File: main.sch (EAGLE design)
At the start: 87 parts, among them Q1 5.8A/30V/35mΩ, Q2 5.8A/30V/35mΩ, Q3 2.5A/30V/105mΩ, U1 BQ24133_RGY_24, U2 SN65HVD32_D_8

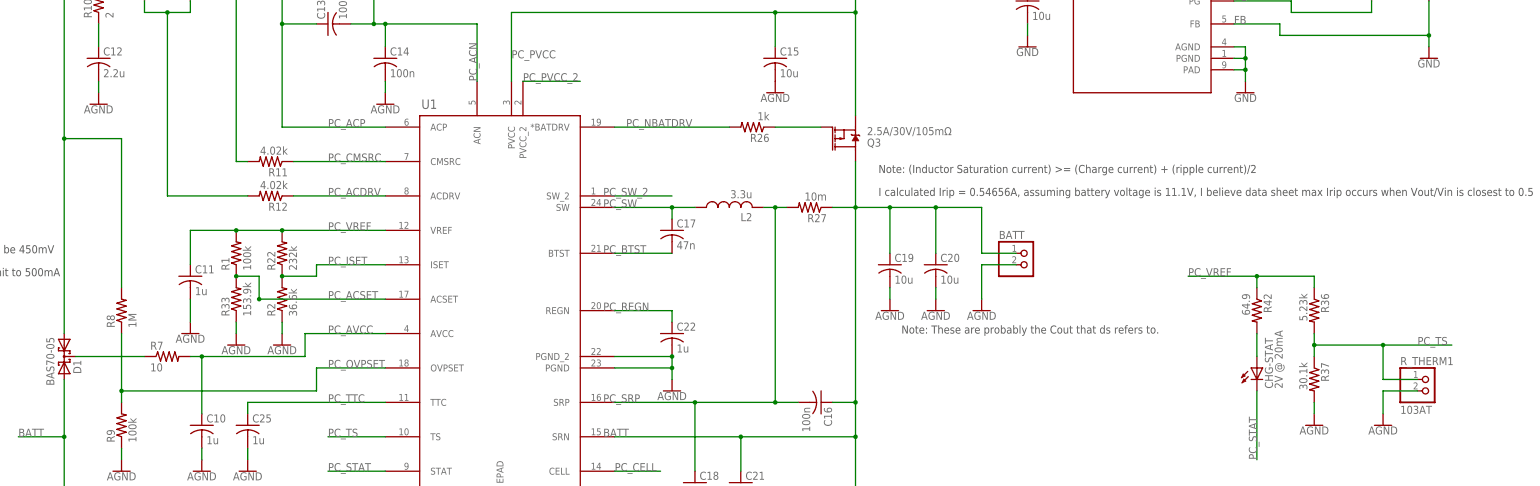
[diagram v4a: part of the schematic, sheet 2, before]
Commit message: Seperated grounds, added pullup to cell pin
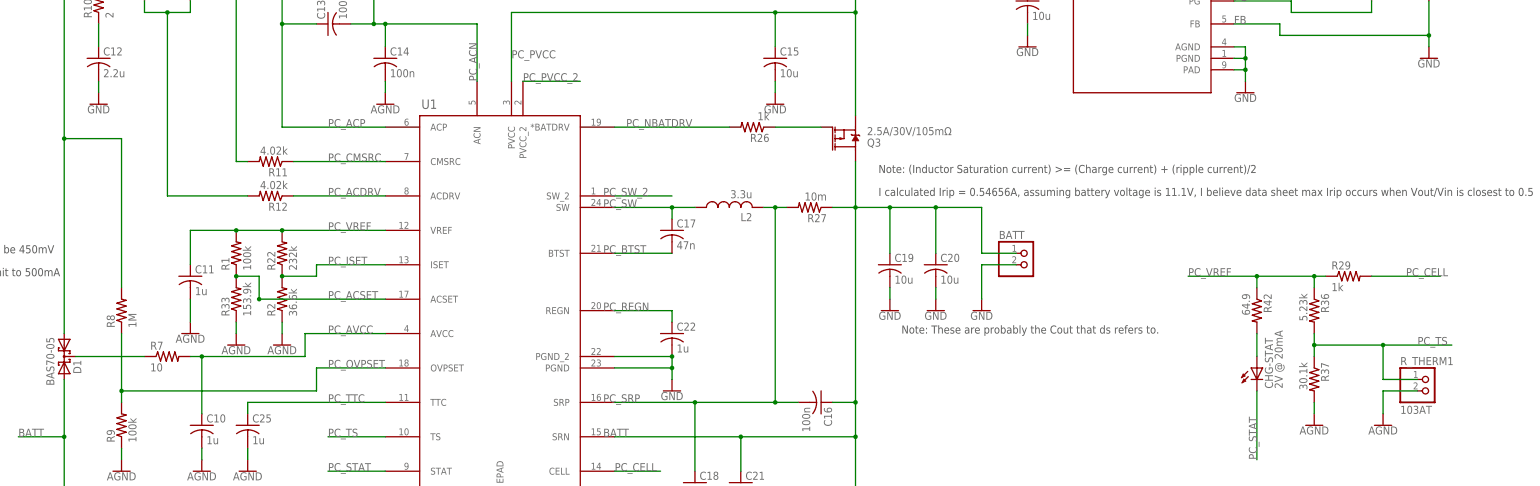
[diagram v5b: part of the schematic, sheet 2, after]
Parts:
- added R29: 1k, resistor:R-US_R0603
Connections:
- net AGND: no longer BATT.2, C12.2, C15.2, C19.2, C20.2, C22.2, U1.PGND, U1.PGND_2
- net GND: now also BATT.2, C12.2, C15.2, C19.2, C20.2, C22.2, U1.PGND, U1.PGND_2
- net PC_CELL: now also R29.2
- net PC_VREF: now also R29.1
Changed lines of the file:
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@@
 <part name="R31" library="resistor" library_urn="urn:adsk.eagle:library:348" deviceset="R-US_" device="R0603" package3d_urn="urn:adsk.eagle:package:26057/1" value="10k"/>
 <part name="SUPPLY6" library="SparkFun-PowerSymbols" deviceset="3.3V" device=""/>
-<part name="U$18" library="SparkFun-PowerSymbols" deviceset="AGND" device=""/>
-<part name="U$19" library="SparkFun-PowerSymbols" deviceset="AGND" device=""/>
-<part name="U$20" library="SparkFun-PowerSymbols" deviceset="AGND" device=""/>
-<part name="U$22" library="SparkFun-PowerSymbols" deviceset="AGND" device=""/>
-<part name="U$23" library="SparkFun-PowerSymbols" deviceset="AGND" device=""/>
-<part name="U$24" library="SparkFun-PowerSymbols" deviceset="AGND" device=""/>
 <part name="SUPPLY9" library="SparkFun-PowerSymbols" deviceset="3.3V" device=""/>
 <part name="GPIO" library="pinhead" library_urn="urn:adsk.eagle:library:325" deviceset="PINHD-1X10" device="" package3d_urn="urn:adsk.eagle:package:22406/2"/>
@@
 <part name="LED1" library="adafruit" deviceset="LED" device="CHIPLED_0603" value="2V @ 20mA"/>
 <part name="SUPPLY11" library="SparkFun-PowerSymbols" deviceset="3.3V" device=""/>
+<part name="GND20" library="SparkFun-PowerSymbols" deviceset="GND" device=""/>
+<part name="GND21" library="SparkFun-PowerSymbols" deviceset="GND" device=""/>
+<part name="GND22" library="SparkFun-PowerSymbols" deviceset="GND" device=""/>
+<part name="GND23" library="SparkFun-PowerSymbols" deviceset="GND" device=""/>
+<part name="GND25" library="SparkFun-PowerSymbols" deviceset="GND" device=""/>
+<part name="GND26" library="SparkFun-PowerSymbols" deviceset="GND" device=""/>
+<part name="R29" library="resistor" library_urn="urn:adsk.eagle:library:348" deviceset="R-US_" device="R0603" package3d_urn="urn:adsk.eagle:package:26057/1" value="1k"/>
 </parts>
 <sheets>
@@
 <instance part="U$15" gate="G$1" x="472.44" y="22.86"/>
 <instance part="U$17" gate="G$1" x="482.6" y="22.86"/>
-<instance part="U$18" gate="G$1" x="467.36" y="53.34"/>
-<instance part="U$19" gate="G$1" x="340.36" y="116.84"/>
-<instance part="U$20" gate="G$1" x="490.22" y="119.38"/>
-<instance part="U$22" gate="G$1" x="535.94" y="71.12"/>
-<instance part="U$23" gate="G$1" x="525.78" y="71.12"/>
-<instance part="U$24" gate="G$1" x="515.62" y="71.12"/>
+<instance part="GND20" gate="1" x="490.22" y="116.84"/>
+<instance part="GND21" gate="1" x="340.36" y="116.84"/>
+<instance part="GND22" gate="1" x="467.36" y="53.34"/>
+<instance part="GND23" gate="1" x="515.62" y="71.12"/>
+<instance part="GND25" gate="1" x="525.78" y="71.12"/>
+<instance part="GND26" gate="1" x="535.94" y="71.12"/>
+<instance part="R29" gate="G$1" x="617.22" y="78.74"/>
 </instances>
 <busses>
@@
 <wire x1="454.66" y1="12.7" x2="454.66" y2="15.24" width="0.1524" layer="91"/>
 <wire x1="454.66" y1="15.24" x2="447.04" y2="15.24" width="0.1524" layer="91"/>
+</segment>
+<segment>
+<pinref part="C15" gate="G$1" pin="2"/>
+<pinref part="GND20" gate="1" pin="GND"/>
+<wire x1="490.22" y1="119.38" x2="490.22" y2="121.92" width="0.1524" layer="91"/>
+</segment>
+<segment>
+<pinref part="C12" gate="G$1" pin="2"/>
+<wire x1="340.36" y1="119.38" x2="340.36" y2="121.92" width="0.1524" layer="91"/>
+<pinref part="GND21" gate="1" pin="GND"/>
+</segment>
+<segment>
+<pinref part="U1" gate="A" pin="PGND"/>
+<pinref part="U1" gate="A" pin="PGND_2"/>
+<wire x1="454.66" y1="60.96" x2="467.36" y2="60.96" width="0.1524" layer="91"/>
+<wire x1="467.36" y1="60.96" x2="467.36" y2="58.42" width="0.1524" layer="91"/>
+<pinref part="C22" gate="G$1" pin="2"/>
+<junction x="467.36" y="60.96"/>
+<wire x1="467.36" y1="58.42" x2="467.36" y2="55.88" width="0.1524" layer="91"/>
+<wire x1="454.66" y1="58.42" x2="467.36" y2="58.42" width="0.1524" layer="91"/>
+<junction x="467.36" y="58.42"/>
+<pinref part="GND22" gate="1" pin="GND"/>
+</segment>
+<segment>
+<pinref part="C19" gate="G$1" pin="2"/>
+<wire x1="515.62" y1="73.66" x2="515.62" y2="76.2" width="0.1524" layer="91"/>
+<pinref part="GND23" gate="1" pin="GND"/>
+</segment>
+<segment>
+<pinref part="C20" gate="G$1" pin="2"/>
+<wire x1="525.78" y1="76.2" x2="525.78" y2="73.66" width="0.1524" layer="91"/>
+<pinref part="GND25" gate="1" pin="GND"/>
+</segment>
+<segment>
+<pinref part="BATT" gate="G$1" pin="2"/>
+<wire x1="543.56" y1="81.28" x2="535.94" y2="81.28" width="0.1524" layer="91"/>
+<wire x1="535.94" y1="81.28" x2="535.94" y2="73.66" width="0.1524" layer="91"/>
+<pinref part="GND26" gate="1" pin="GND"/>
 </segment>
 </net>
@@
 <junction x="596.9" y="78.74"/>
 <label x="581.66" y="78.74" size="1.778" layer="95"/>
+<pinref part="R29" gate="G$1" pin="1"/>
+<wire x1="609.6" y1="78.74" x2="612.14" y2="78.74" width="0.1524" layer="91"/>
+<junction x="609.6" y="78.74"/>
 </segment>
 </net>
@@
 <label x="454.66" y="35.56" size="1.778" layer="95"/>
 </segment>
+<segment>
+<pinref part="R29" gate="G$1" pin="2"/>
+<wire x1="622.3" y1="78.74" x2="637.54" y2="78.74" width="0.1524" layer="91"/>
+<label x="629.92" y="78.74" size="1.778" layer="95"/>
+</segment>
 </net>
 <net name="PC_PVCC_2" class="0">
@@
 <pinref part="U$17" gate="G$1" pin="AGND"/>
 </segment>
-<segment>
-<pinref part="U1" gate="A" pin="PGND"/>
-<pinref part="U1" gate="A" pin="PGND_2"/>
-<wire x1="454.66" y1="60.96" x2="467.36" y2="60.96" width="0.1524" layer="91"/>
-<wire x1="467.36" y1="60.96" x2="467.36" y2="58.42" width="0.1524" layer="91"/>
-<pinref part="C22" gate="G$1" pin="2"/>
-<junction x="467.36" y="60.96"/>
-<wire x1="467.36" y1="58.42" x2="467.36" y2="55.88" width="0.1524" layer="91"/>
-<wire x1="454.66" y1="58.42" x2="467.36" y2="58.42" width="0.1524" layer="91"/>
-<junction x="467.36" y="58.42"/>
-<pinref part="U$18" gate="G$1" pin="AGND"/>
-</segment>
-<segment>
-<pinref part="C12" gate="G$1" pin="2"/>
-<wire x1="340.36" y1="119.38" x2="340.36" y2="121.92" width="0.1524" layer="91"/>
-<pinref part="U$19" gate="G$1" pin="AGND"/>
-</segment>
-<segment>
-<pinref part="C15" gate="G$1" pin="2"/>
-<pinref part="U$20" gate="G$1" pin="AGND"/>
-</segment>
-<segment>
-<pinref part="BATT" gate="G$1" pin="2"/>
-<wire x1="543.56" y1="81.28" x2="535.94" y2="81.28" width="0.1524" layer="91"/>
-<wire x1="535.94" y1="81.28" x2="535.94" y2="73.66" width="0.1524" layer="91"/>
-<pinref part="U$22" gate="G$1" pin="AGND"/>
-</segment>
-<segment>
-<pinref part="C20" gate="G$1" pin="2"/>
-<wire x1="525.78" y1="76.2" x2="525.78" y2="73.66" width="0.1524" layer="91"/>
-<pinref part="U$23" gate="G$1" pin="AGND"/>
-</segment>
-<segment>
-<pinref part="C19" gate="G$1" pin="2"/>
-<wire x1="515.62" y1="73.66" x2="515.62" y2="76.2" width="0.1524" layer="91"/>
-<pinref part="U$24" gate="G$1" pin="AGND"/>
-</segment>
-</net>
+</net>

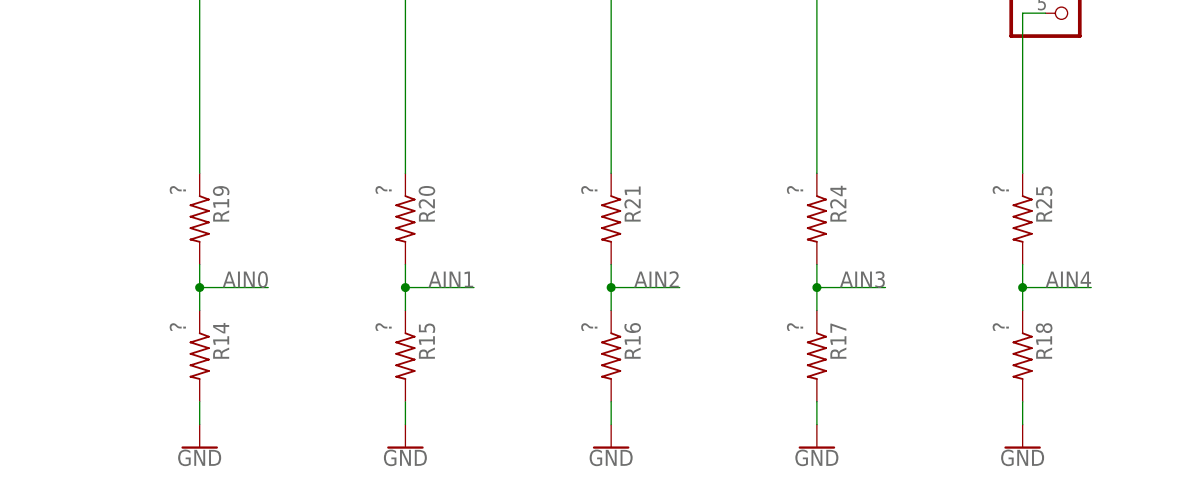
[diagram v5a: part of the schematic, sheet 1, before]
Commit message: Set adc voltage divider values
Used 100ohm output impedance of ducers and 3.5kohm limit in samd21 datasheet to arrive at the vdiv resistor values.
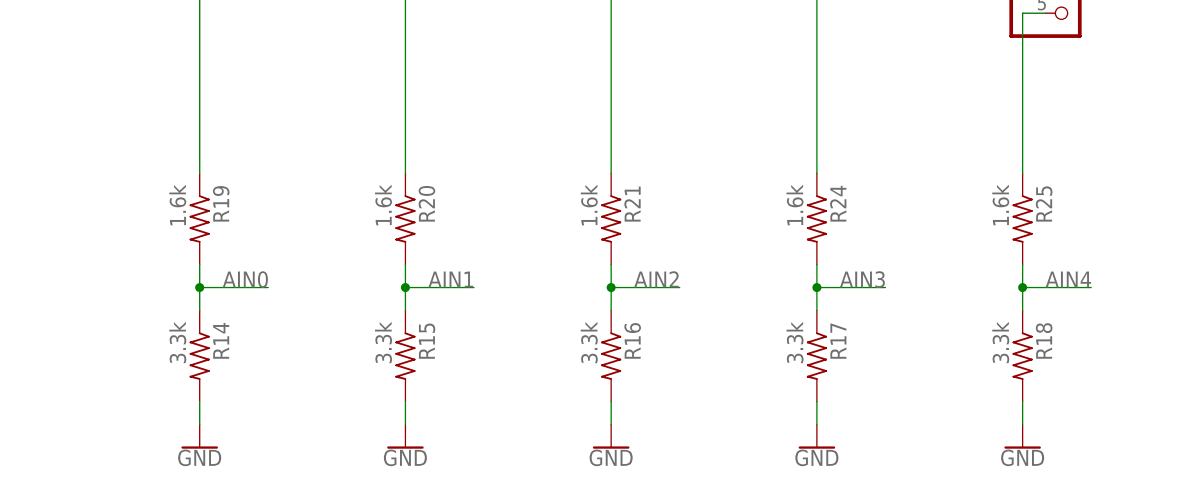
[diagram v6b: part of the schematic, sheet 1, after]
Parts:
- R14, R15, R16, R17, R18: value ? -> 3.3k
- R19, R20, R21, R24, R25: value ? -> 1.6k
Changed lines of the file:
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@@
 <part name="GND17" library="SparkFun-PowerSymbols" deviceset="GND" device=""/>
 <part name="GND18" library="SparkFun-PowerSymbols" deviceset="GND" device=""/>
-<part name="R14" library="resistor" library_urn="urn:adsk.eagle:library:348" deviceset="R-US_" device="R0603" package3d_urn="urn:adsk.eagle:package:26057/1" value="?"/>
-<part name="R15" library="resistor" library_urn="urn:adsk.eagle:library:348" deviceset="R-US_" device="R0603" package3d_urn="urn:adsk.eagle:package:26057/1" value="?"/>
-<part name="R16" library="resistor" library_urn="urn:adsk.eagle:library:348" deviceset="R-US_" device="R0603" package3d_urn="urn:adsk.eagle:package:26057/1" value="?"/>
-<part name="R17" library="resistor" library_urn="urn:adsk.eagle:library:348" deviceset="R-US_" device="R0603" package3d_urn="urn:adsk.eagle:package:26057/1" value="?"/>
-<part name="R18" library="resistor" library_urn="urn:adsk.eagle:library:348" deviceset="R-US_" device="R0603" package3d_urn="urn:adsk.eagle:package:26057/1" value="?"/>
-<part name="R19" library="resistor" library_urn="urn:adsk.eagle:library:348" deviceset="R-US_" device="R0603" package3d_urn="urn:adsk.eagle:package:26057/1" value="?"/>
-<part name="R20" library="resistor" library_urn="urn:adsk.eagle:library:348" deviceset="R-US_" device="R0603" package3d_urn="urn:adsk.eagle:package:26057/1" value="?"/>
-<part name="R21" library="resistor" library_urn="urn:adsk.eagle:library:348" deviceset="R-US_" device="R0603" package3d_urn="urn:adsk.eagle:package:26057/1" value="?"/>
-<part name="R24" library="resistor" library_urn="urn:adsk.eagle:library:348" deviceset="R-US_" device="R0603" package3d_urn="urn:adsk.eagle:package:26057/1" value="?"/>
-<part name="R25" library="resistor" library_urn="urn:adsk.eagle:library:348" deviceset="R-US_" device="R0603" package3d_urn="urn:adsk.eagle:package:26057/1" value="?"/>
+<part name="R14" library="resistor" library_urn="urn:adsk.eagle:library:348" deviceset="R-US_" device="R0603" package3d_urn="urn:adsk.eagle:package:26057/1" value="3.3k"/>
+<part name="R15" library="resistor" library_urn="urn:adsk.eagle:library:348" deviceset="R-US_" device="R0603" package3d_urn="urn:adsk.eagle:package:26057/1" value="3.3k"/>
+<part name="R16" library="resistor" library_urn="urn:adsk.eagle:library:348" deviceset="R-US_" device="R0603" package3d_urn="urn:adsk.eagle:package:26057/1" value="3.3k"/>
+<part name="R17" library="resistor" library_urn="urn:adsk.eagle:library:348" deviceset="R-US_" device="R0603" package3d_urn="urn:adsk.eagle:package:26057/1" value="3.3k"/>
+<part name="R18" library="resistor" library_urn="urn:adsk.eagle:library:348" deviceset="R-US_" device="R0603" package3d_urn="urn:adsk.eagle:package:26057/1" value="3.3k"/>
+<part name="R19" library="resistor" library_urn="urn:adsk.eagle:library:348" deviceset="R-US_" device="R0603" package3d_urn="urn:adsk.eagle:package:26057/1" value="1.6k"/>
+<part name="R20" library="resistor" library_urn="urn:adsk.eagle:library:348" deviceset="R-US_" device="R0603" package3d_urn="urn:adsk.eagle:package:26057/1" value="1.6k"/>
+<part name="R21" library="resistor" library_urn="urn:adsk.eagle:library:348" deviceset="R-US_" device="R0603" package3d_urn="urn:adsk.eagle:package:26057/1" value="1.6k"/>
+<part name="R24" library="resistor" library_urn="urn:adsk.eagle:library:348" deviceset="R-US_" device="R0603" package3d_urn="urn:adsk.eagle:package:26057/1" value="1.6k"/>
+<part name="R25" library="resistor" library_urn="urn:adsk.eagle:library:348" deviceset="R-US_" device="R0603" package3d_urn="urn:adsk.eagle:package:26057/1" value="1.6k"/>
 <part name="GND5" library="SparkFun-PowerSymbols" deviceset="GND" device=""/>
 <part name="IMU" library="BNO055" deviceset="BNO055" device=""/>

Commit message: Routing
Need to choose L and sizes for caps and res
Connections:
- net PC_AVCC renamed N$21
- net PC_NBATDRV renamed *BATDRV
- net PC_STAT: now also R36.2, R37.1, R_THERM1.1
- net PC_TS: no longer R36.2, R37.1, R_THERM1.1
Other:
- moved on the sheet: C22, CHG-STAT, R1, R22, R29, R36, R37, R42, R_THERM1

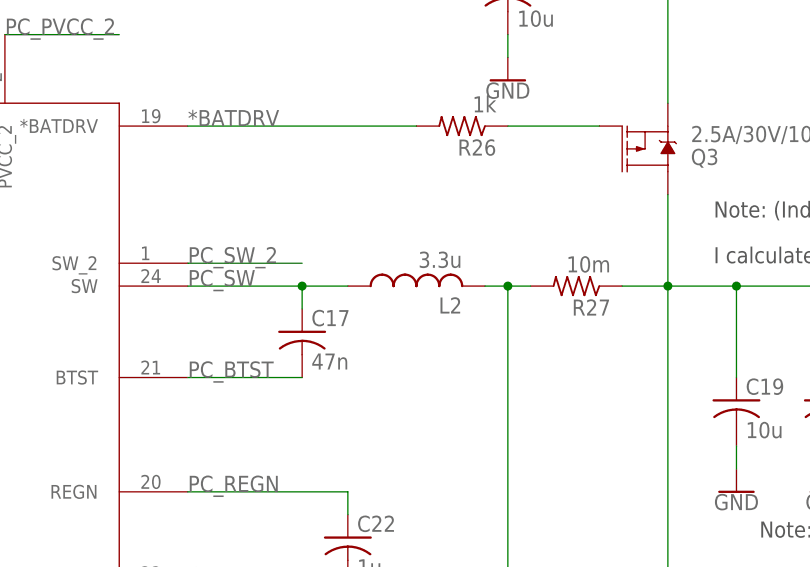
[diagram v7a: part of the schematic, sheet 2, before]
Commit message: Still need to change pad sizes
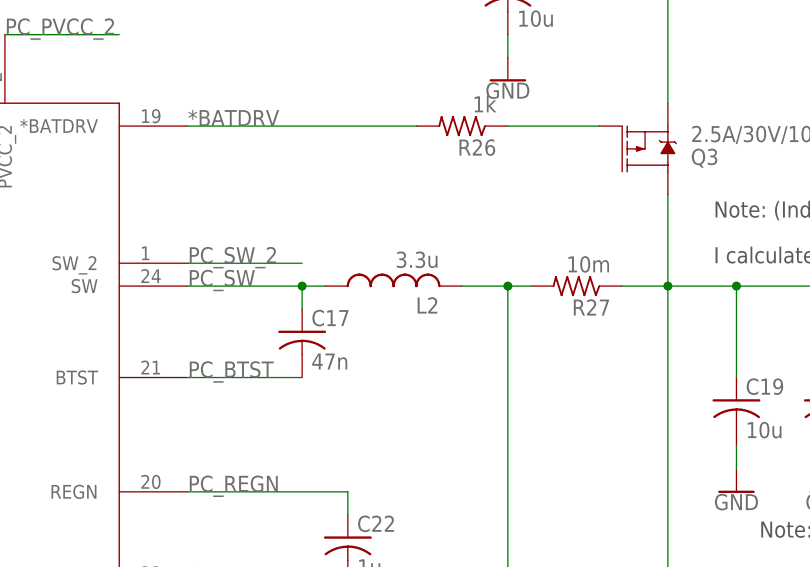
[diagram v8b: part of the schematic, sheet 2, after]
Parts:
- L2: device resistor:L-USL2012C -> rcl:L-USL3225M
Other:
- moved on the sheet: L2
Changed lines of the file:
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@@
 <?xml version="1.0" encoding="utf-8"?>
 <!DOCTYPE eagle SYSTEM "eagle.dtd">
-<eagle version="8.6.0">
+<eagle version="8.5.1">
 <drawing>
 <settings>
@@
 <part name="Q3" library="SparkFun-DiscreteSemi" deviceset="MOSFET_PCH" device="-DMG2307L" value="2.5A/30V/105mΩ"/>
 <part name="R26" library="resistor" deviceset="R-US_" device="R0603" value="1k"/>
-<part name="L2" library="resistor" deviceset="L-US" device="L2012C" value="3.3u"/>
+<part name="L2" library="rcl" library_urn="urn:adsk.eagle:library:334" deviceset="L-US" device="L3225M" package3d_urn="urn:adsk.eagle:package:23477/1" value="3.3u"/>
 <part name="R27" library="resistor" deviceset="R-US_" device="R0603" value="10m"/>
 <part name="C16" library="resistor" deviceset="C-US" device="C0603" value="100n"/>
@@
 <instance part="Q3" gate="G$1" x="505.46" y="109.22" rot="MR180"/>
 <instance part="R26" gate="G$1" x="485.14" y="111.76" rot="R180"/>
-<instance part="L2" gate="G$1" x="480.06" y="93.98" rot="R90"/>
+<instance part="L2" gate="G$1" x="477.52" y="93.98" rot="R90"/>
 <instance part="R27" gate="G$1" x="497.84" y="93.98" rot="R180"/>
 <instance part="C16" gate="G$1" x="500.38" y="50.8" rot="R270"/>
@@
 <pinref part="L2" gate="G$1" pin="2"/>
 <pinref part="R27" gate="G$1" pin="2"/>
-<wire x1="487.68" y1="93.98" x2="490.22" y2="93.98" width="0.1524" layer="91"/>
+<wire x1="485.14" y1="93.98" x2="490.22" y2="93.98" width="0.1524" layer="91"/>
 <wire x1="490.22" y1="93.98" x2="492.76" y2="93.98" width="0.1524" layer="91"/>
 <junction x="490.22" y="93.98"/>
@@
 <pinref part="L2" gate="G$1" pin="1"/>
 <pinref part="C17" gate="G$1" pin="1"/>
-<wire x1="472.44" y1="93.98" x2="467.36" y2="93.98" width="0.1524" layer="91"/>
+<wire x1="469.9" y1="93.98" x2="467.36" y2="93.98" width="0.1524" layer="91"/>
 <wire x1="467.36" y1="93.98" x2="467.36" y2="91.44" width="0.1524" layer="91"/>
 <pinref part="U1" gate="A" pin="SW"/>
@@
 </schematic>
 </drawing>
+<compatibility>
+<note version="8.2" severity="warning">
+Since Version 8.2, EAGLE supports online libraries. The ids
+of those online libraries will not be understood (or retained)
+with this version.
+</note>
+<note version="8.3" severity="warning">
+Since Version 8.3, EAGLE supports URNs for individual library
+assets (packages, symbols, and devices). The URNs of those assets
+will not be understood (or retained) with this version.
+</note>
+<note version="8.3" severity="warning">
+Since Version 8.3, EAGLE supports the association of 3D packages
+with devices in libraries, schematics, and board files. Those 3D
+packages will not be understood (or retained) with this version.
+</note>
+<note version="8.4" severity="warning">
+Since Version 8.4, EAGLE supports properties for SPICE simulation.
+Probes in schematics and SPICE mapping objects found in parts and library devices
+will not be understood with this version. Update EAGLE to the latest version
+for full support of SPICE simulation.
+</note>
+</compatibility>
 </eagle>
